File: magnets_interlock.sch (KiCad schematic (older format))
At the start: 9 parts

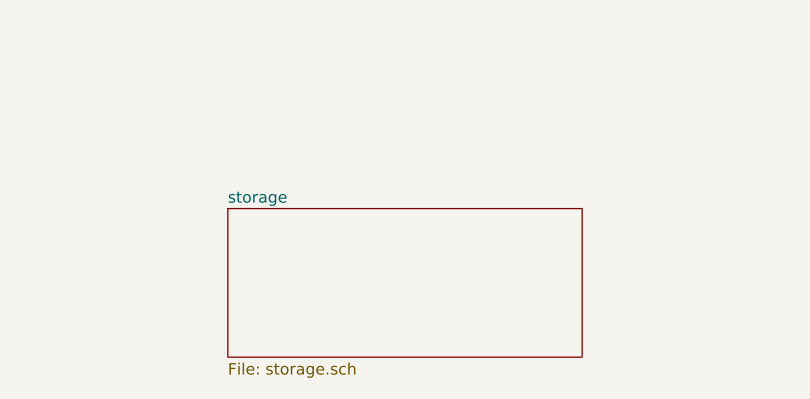
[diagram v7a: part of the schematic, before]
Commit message: Made 5V local label to each sheet
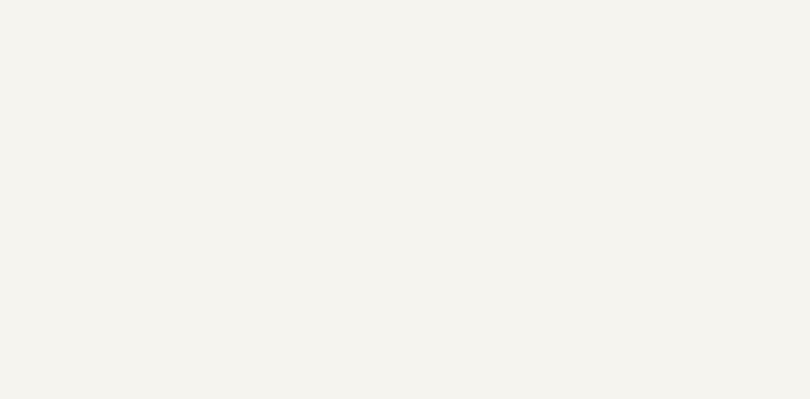
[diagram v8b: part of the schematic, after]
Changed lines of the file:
@@
 $Descr A4 11693 8268
 encoding utf-8
-Sheet 1 3
+Sheet 1 2
 Title ""
 Date ""
@@
 	-1   0    0    -1
 $EndComp
-$Sheet
-S 4200 6500 1550 650
-U 5EF82676
-F0 "storage" 50
-F1 "storage.sch" 50
-$EndSheet
 Text GLabel 1450 1400 2    50   Input ~ 0
 +5VIN
@@
 	2650 3050 2400 3050
 $Comp
-L power:GND #PWR?
+L power:GND #PWR0101
 U 1 1 5EFAC57B
 P 2600 3250
-F 0 "#PWR?" H 2600 3000 50  0001 C CNN
+F 0 "#PWR0101" H 2600 3000 50  0001 C CNN
 F 1 "GND" H 2605 3077 50  0000 C CNN
 F 2 "" H 2600 3250 50  0001 C CNN
@@
 	2600 3250 2400 3250
 $Comp
-L power:GND #PWR?
+L power:GND #PWR0102
 U 1 1 5EFACEA7
 P 2650 4200
-F 0 "#PWR?" H 2650 3950 50  0001 C CNN
+F 0 "#PWR0102" H 2650 3950 50  0001 C CNN
 F 1 "GND" H 2655 4027 50  0000 C CNN
 F 2 "" H 2650 4200 50  0001 C CNN
@@
 Connection ~ 6450 1600
 $Comp
-L power:GND #PWR?
+L power:GND #PWR0103
 U 1 1 5EFAE3FF
 P 6700 1800
-F 0 "#PWR?" H 6700 1550 50  0001 C CNN
+F 0 "#PWR0103" H 6700 1550 50  0001 C CNN
 F 1 "GND" H 6705 1627 50  0000 C CNN
 F 2 "" H 6700 1800 50  0001 C CNN
@@
 Connection ~ 6550 1800
 $Comp
-L power:GND #PWR?
+L power:GND #PWR0104
 U 1 1 5EFAECA0
 P 6650 1200
-F 0 "#PWR?" H 6650 950 50  0001 C CNN
+F 0 "#PWR0104" H 6650 950 50  0001 C CNN
 F 1 "GND" V 6655 1072 50  0000 R CNN
 F 2 "" H 6650 1200 50  0001 C CNN
@@
 	6650 1100 6450 1100
 $Comp
-L power:GND #PWR?
+L power:GND #PWR0105
 U 1 1 5EFB00AF
 P 8400 1400
-F 0 "#PWR?" H 8400 1150 50  0001 C CNN
+F 0 "#PWR0105" H 8400 1150 50  0001 C CNN
 F 1 "GND" H 8405 1227 50  0000 C CNN
 F 2 "" H 8400 1400 50  0001 C CNN
@@
 $EndComp
 $Comp
-L power:GND #PWR?
+L power:GND #PWR0106
 U 1 1 5EFB1CED
 P 8050 700
-F 0 "#PWR?" H 8050 450 50  0001 C CNN
+F 0 "#PWR0106" H 8050 450 50  0001 C CNN
 F 1 "GND" V 8055 572 50  0000 R CNN
 F 2 "" H 8050 700 50  0001 C CNN
